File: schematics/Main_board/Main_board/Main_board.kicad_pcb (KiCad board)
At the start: 2 copper layers, 7 parts, among them J1 USB_B_Micro, J2 Conn_01x16_Female, U1 ESP32-S3-WROOM-1, U2 AP2112K-3.3, U3 AP9101CK6, U4 CH340G, U5 PCF8563T

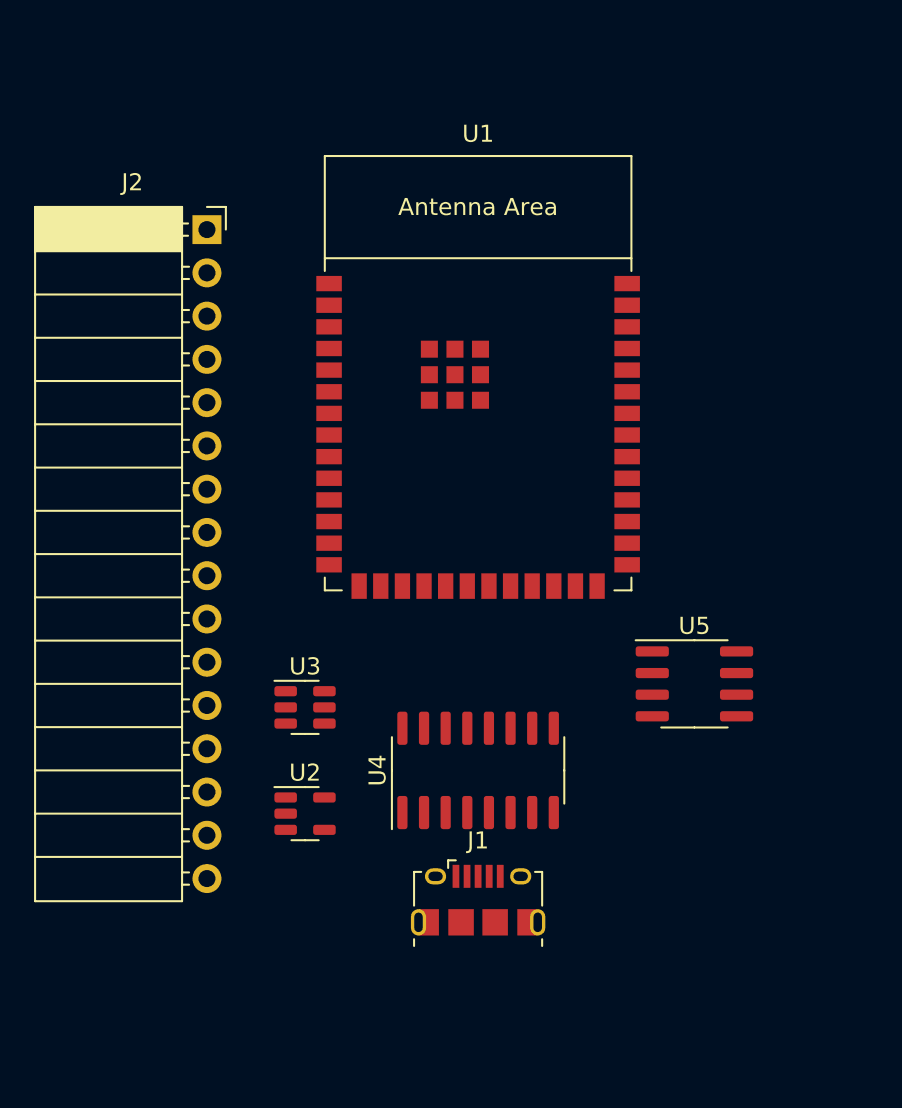
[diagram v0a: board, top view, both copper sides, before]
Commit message: Update: Added LCD symbol
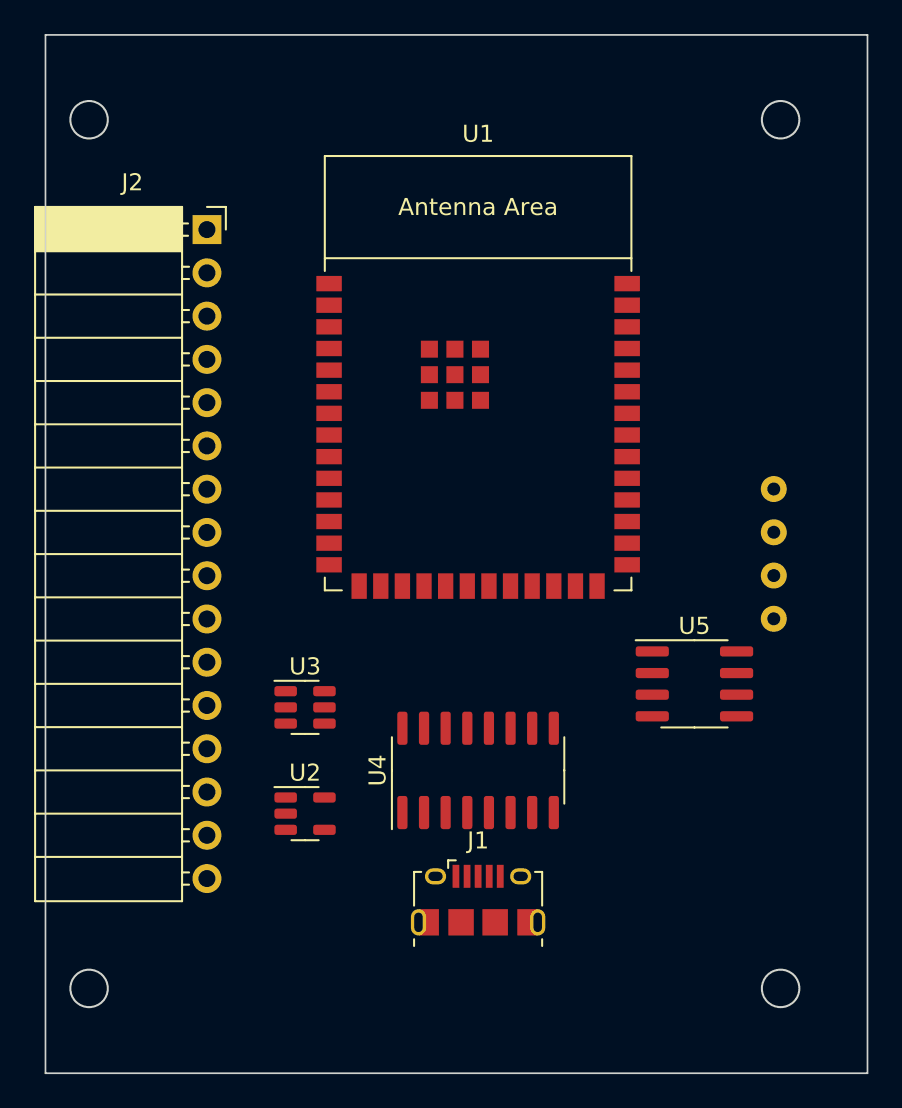
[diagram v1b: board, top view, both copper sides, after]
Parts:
- added U6: LCD, LCD:LCD_IIC_12864, B.Cu at (124.5, 73.7)
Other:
- board outline added: 48.3 x 61 mm
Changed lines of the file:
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@@
   (net 95 "unconnected-(U5-Pad7)")
   (net 96 "unconnected-(U5-Pad8)")
+  (net 97 "unconnected-(U6-Pad1)")
+  (net 98 "unconnected-(U6-Pad2)")
+  (net 99 "unconnected-(U6-Pad3)")
+  (net 100 "unconnected-(U6-Pad4)")
   (footprint "Connector_PinSocket_2.54mm:PinSocket_1x16_P2.54mm_Horizontal" (layer "F.Cu")
     (at 111.08 54.61)
@@
     (pad "6" thru_hole oval (at -2.5 -1.4) (size 1.25 0.95) (drill oval 0.85 0.55) (layers *.Cu *.Mask)
       (net 45 "unconnected-(J1-Pad6)") (pinfunction "Shield") (pintype "passive"))
-    (model "${KICAD6_3DMODEL_DIR}/Connector_USB.3dshapes/USB_Micro-B_Amphenol_10118194_Horizontal.wrl"
-      (offset (xyz 0 0 0))
-      (scale (xyz 1 1 1))
-      (rotate (xyz 0 0 0))
-    )
   )
   (footprint "Package_SO:SOIC-16_3.9x9.9mm_P1.27mm" (layer "F.Cu")
@@
     )
   )
+  (footprint "LCD:LCD_IIC_12864" (layer "B.Cu")
+    (at 124.46 73.66 90)
+    (property "Sheetfile" "Main_board.kicad_sch")
+    (property "Sheetname" "")
+    (attr through_hole)
+    (fp_text reference "U6" (at 0 0.5 270 unlocked) (layer "B.SilkS")
+      (effects (font (size 1 1) (thickness 0.15)) (justify mirror))
+    )
+    (fp_text value "LCD" (at 0 -1 270 unlocked) (layer "B.Fab")
+      (effects (font (size 1 1) (thickness 0.15)) (justify mirror))
+    )
+    (fp_text user "LCD SCREEN 128 64" (at 0 -5.08 270 unlocked) (layer "B.SilkS")
+      (effects (font (size 1 1) (thickness 0.15)) (justify mirror))
+    )
+    (fp_text user "${REFERENCE}" (at 0 -2.5 270 unlocked) (layer "B.Fab")
+      (effects (font (size 1 1) (thickness 0.15)) (justify mirror))
+    )
+    (fp_rect (start -26.8 17.78) (end 26.8 -17.78) (layer "B.SilkS") (width 0.12) (fill none))
+    (fp_rect (start -28.5 22.8) (end 28.5 -22.8) (layer "B.SilkS") (width 0.12) (fill none))
+    (fp_circle (center 25.5 20.3) (end 26.6 20.3) (layer "Edge.Cuts") (width 0.12) (fill solid))
+    (fp_circle (center -25.5 -20.3) (end -24.4 -20.3) (layer "Edge.Cuts") (width 0.12) (fill solid))
+    (fp_circle (center 25.5 -20.3) (end 26.6 -20.3) (layer "Edge.Cuts") (width 0.12) (fill solid))
+    (fp_circle (center -25.5 20.3) (end -24.4 20.3) (layer "Edge.Cuts") (width 0.12) (fill solid))
+    (pad "1" thru_hole circle (at -3.8 19.9 90) (size 1.524 1.524) (drill 0.762) (layers *.Cu *.Mask)
+      (net 97 "unconnected-(U6-Pad1)") (pinfunction "SDA") (pintype "input"))
+    (pad "2" thru_hole circle (at -1.26 19.9 90) (size 1.524 1.524) (drill 0.762) (layers *.Cu *.Mask)
+      (net 98 "unconnected-(U6-Pad2)") (pinfunction "SCL") (pintype "input"))
+    (pad "3" thru_hole circle (at 3.82 19.9 90) (size 1.524 1.524) (drill 0.762) (layers *.Cu *.Mask)
+      (net 99 "unconnected-(U6-Pad3)") (pinfunction "GND") (pintype "power_in"))
+    (pad "4" thru_hole circle (at 1.28 19.9 90) (size 1.524 1.524) (drill 0.762) (layers *.Cu *.Mask)
+      (net 100 "unconnected-(U6-Pad4)") (pinfunction "Vcc") (pintype "power_in"))
+    (model "/home/jose/Documentos/Projects/Watchdog/ESP32-watchdog/3dComponents/LCD screen-Part.step"
+      (offset (xyz 0 0 2.5))
+      (scale (xyz 1 1 1))
+      (rotate (xyz 0 0 0))
+    )
+  )
+  (gr_rect (start 101.6 43.18) (end 149.86 104.14) (layer "Edge.Cuts") (width 0.1) (fill none))
 )

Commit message: Update: added new schematics components
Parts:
- added BT1: 1v5 LR44, LCD:MY-LR44-02, B.Cu at (137.2, 111.3)
- added C1: 1uf, Capacitor_SMD:C_0201_0603Metric, F.Cu at (139.7, 62.7)
- added C2: 1uf, Capacitor_SMD:C_0201_0603Metric, F.Cu at (142.2, 59.2)
- added C3: 1uf, Capacitor_SMD:C_0201_0603Metric, F.Cu at (142.2, 61.0)
- added C4: 33p, Capacitor_SMD:C_0201_0603Metric, F.Cu at (139.7, 59.2)
- added C5: 33p, Capacitor_SMD:C_0201_0603Metric, F.Cu at (142.2, 62.7)
- added C6: 0.1u, Capacitor_SMD:C_0201_0603Metric, F.Cu at (139.7, 61.0)
- added C7: 0.1u, Capacitor_SMD:C_0201_0603Metric, F.Cu at (144.6, 59.2)
- added U7: LIS3DH, Package_LGA:LGA-16_3x3mm_P0.5mm_LayoutBorder3x5y, F.Cu at (144.8, 66.0)
- added Y1: 12Mhz, Crystal:Resonator_SMD_Murata_CSTxExxV-3Pin_3.0x1.1mm_HandSoldering, F.Cu at (140.7, 88.9)
- added Y2: 32.768kHz, Crystal:Crystal_C38-LF_D3.0mm_L8.0mm_Horizontal, F.Cu at (114.3, 40.6)
- U3: value AP9101CK6 -> BQ21040DBVR
- moved U1 12.7 mm to (127.0, 53.3)
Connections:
- J1 pad 1: unconnected-(J1-Pad1) -> +5V
- J1 pad 2: unconnected-(J1-Pad2) -> /D-
- J1 pad 3: unconnected-(J1-Pad3) -> /D+
- J1 pad 4: unconnected-(J1-Pad4) -> GNDREF
- J1 pad 5: unconnected-(J1-Pad5) -> GNDREF
- J1 pad 6: unconnected-(J1-Pad6) -> GNDREF
- J2 pad 1: unconnected-(J2-Pad1) -> +3V3
- J2 pad 10: unconnected-(J2-Pad10) -> /I/O_1
- J2 pad 11: unconnected-(J2-Pad11) -> /I/O_2
- J2 pad 12: unconnected-(J2-Pad12) -> /I/O_3
- J2 pad 13: unconnected-(J2-Pad13) -> /I/O_4
- J2 pad 14: unconnected-(J2-Pad14) -> /I/O_5
- J2 pad 15: unconnected-(J2-Pad15) -> GNDREF
- J2 pad 16: unconnected-(J2-Pad16) -> GNDREF
- J2 pad 2: unconnected-(J2-Pad2) -> +3V3
- J2 pad 3: unconnected-(J2-Pad3) -> /UART_TX
- J2 pad 4: unconnected-(J2-Pad4) -> /UART_RX
- J2 pad 5: unconnected-(J2-Pad5) -> /MOSI
- J2 pad 6: unconnected-(J2-Pad6) -> /MISO
- J2 pad 7: unconnected-(J2-Pad7) -> /CLK
- J2 pad 8: unconnected-(J2-Pad8) -> /SDA_2
- J2 pad 9: unconnected-(J2-Pad9) -> /SCL_2
- U1 pad 36: unconnected-(U1-Pad36) -> /UART_TX0_PGR
- U1 pad 37: unconnected-(U1-Pad37) -> /UART_RX0_PGR
- U2 pad 1: unconnected-(U2-Pad1) -> +BATT
- U2 pad 2: unconnected-(U2-Pad2) -> GNDREF
- U2 pad 3: unconnected-(U2-Pad3) -> +BATT
- U2 pad 5: unconnected-(U2-Pad5) -> +3V3
- U3 pad 5: unconnected-(U3-Pad5) -> Net-(C3-Pad1)
- U3 pad 6: unconnected-(U3-Pad6) -> GNDREF
- U4 pad 1: unconnected-(U4-Pad1) -> GNDREF
- U4 pad 16: unconnected-(U4-Pad16) -> +5V
- U4 pad 2: unconnected-(U4-Pad2) -> /UART_TX0_PGR
- U4 pad 3: unconnected-(U4-Pad3) -> /UART_RX0_PGR
- U4 pad 4: unconnected-(U4-Pad4) -> Net-(C6-Pad2)
- U4 pad 5: unconnected-(U4-Pad5) -> /D+
- U4 pad 6: unconnected-(U4-Pad6) -> /D-
- U4 pad 7: unconnected-(U4-Pad7) -> Net-(C5-Pad1)
- U4 pad 8: unconnected-(U4-Pad8) -> Net-(C4-Pad1)
- U6 pad 1: unconnected-(U6-Pad1) -> /SDA_1
- U6 pad 2: unconnected-(U6-Pad2) -> /SCL_1
- U6 pad 3: unconnected-(U6-Pad3) -> GNDREF
- U6 pad 4: unconnected-(U6-Pad4) -> +3V3
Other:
- board size 48.3 x 61 mm -> 48.3 x 78.7 mm
- copper layers 2 -> 4

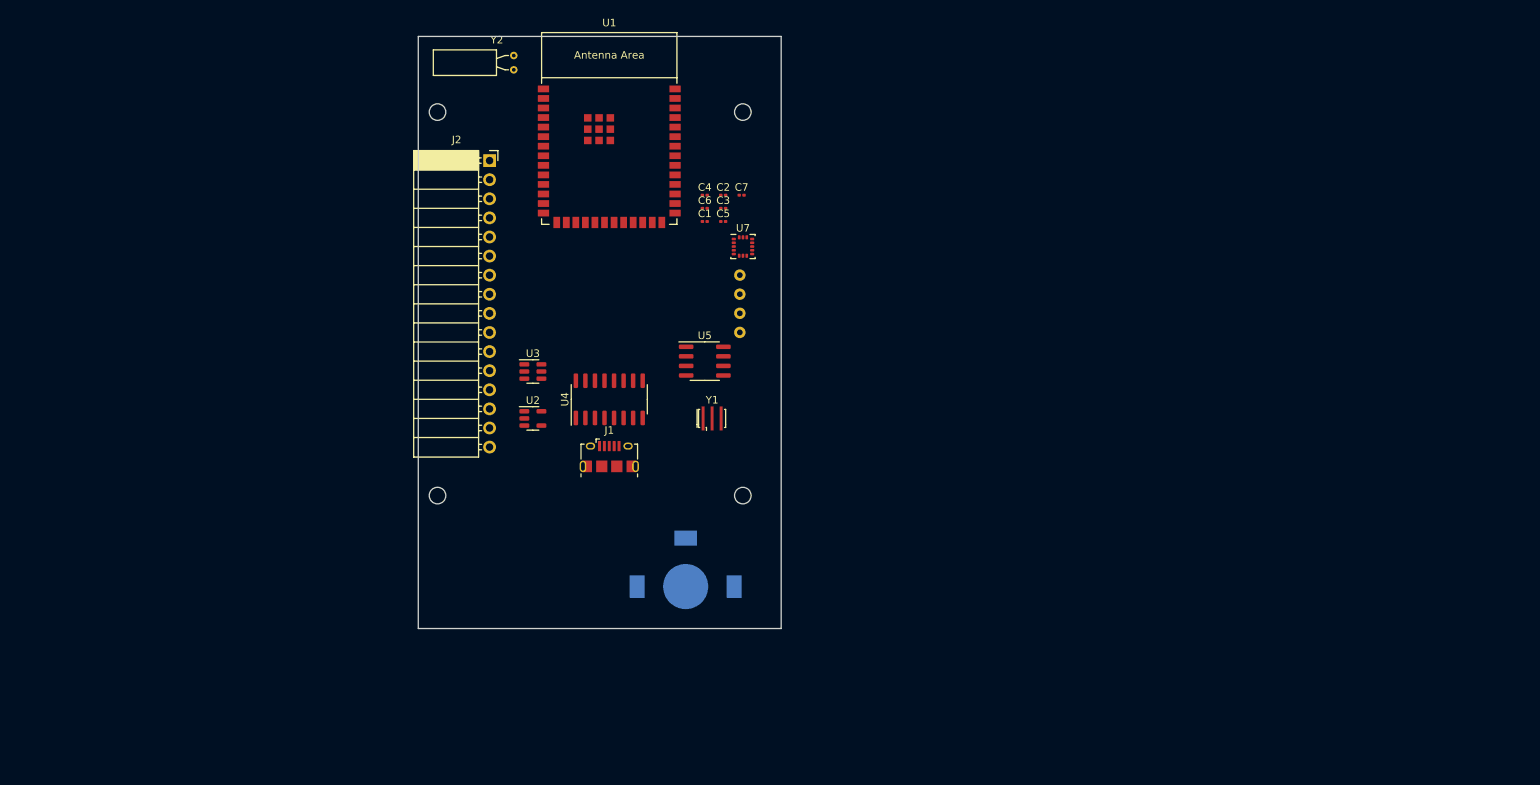
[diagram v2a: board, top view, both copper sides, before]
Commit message: Update: add components to schematics
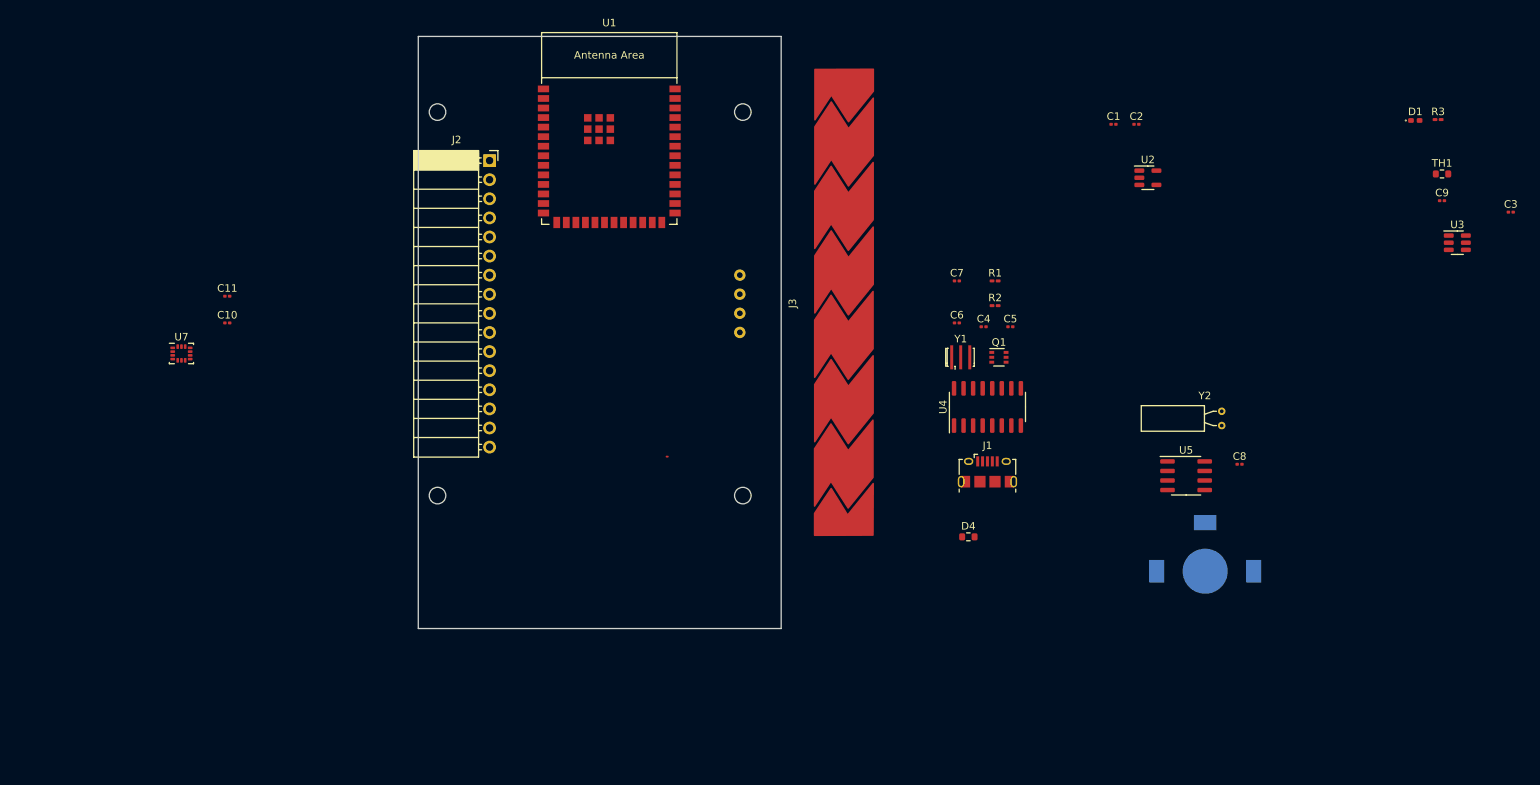
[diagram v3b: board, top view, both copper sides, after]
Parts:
- added C10: 100nf, Capacitor_SMD:C_0201_0603Metric, F.Cu at (76.2, 76.2)
- added C11: 100nf, Capacitor_SMD:C_0201_0603Metric, F.Cu at (76.2, 72.6)
- added C8: 8p, Capacitor_SMD:C_0201_0603Metric, F.Cu at (210.8, 95.0)
- added C9: 1uf, Capacitor_SMD:C_0201_0603Metric, F.Cu at (237.7, 59.9)
- added D1: LED, LED_SMD:LED_0402_1005Metric_Pad0.77x0.64mm_HandSolder, F.Cu at (234.2, 49.3)
- added D4: TPD1E10B06DPYR, Resistor_SMD:R_0603_1608Metric, F.Cu at (174.8, 104.6)
- added J3: TOUCH, LCD:slide_sensor_8p, F.Cu at (159.5, 73.7)
- added Q1: UMH3N, Package_TO_SOT_SMD:SOT-363_SC-70-6, F.Cu at (178.8, 80.8)
- added R1: 1K, Resistor_SMD:R_0201_0603Metric_Pad0.64x0.40mm_HandSolder, F.Cu at (178.3, 70.6)
- added R2: 10k, Resistor_SMD:R_0201_0603Metric_Pad0.64x0.40mm_HandSolder, F.Cu at (178.3, 73.9)
- added R3: 120, Resistor_SMD:R_0201_0603Metric_Pad0.64x0.40mm_HandSolder, F.Cu at (237.2, 49.2)
- added TH1: NCP18XH103F03RB, Resistor_SMD:R_0603_1608Metric, F.Cu at (237.7, 56.4)
- U7: value LIS3DH -> LSM6DS3; footprint Package_LGA:LGA-16_3x3mm_P0.5mm_LayoutBorder3x5y -> Package_LGA:LGA-14_3x2.5mm_P0.5mm_LayoutBorder3x4y
- moved U3 124.1 mm to (239.8, 65.5)
- moved Y2 105.4 mm to (208.4, 88.0)
- moved C3 104.7 mm to (246.9, 61.5)
- moved U2 87.8 mm to (198.6, 56.9)
- moved U7 76.0 mm to (70.1, 80.3)
- moved BT1 69.1 mm to (206.2, 109.2)
- moved U5 65.8 mm to (203.7, 96.5)
- moved C1 55.9 mm to (194.1, 49.8)
- moved C2 55.8 mm to (197.1, 49.8)
- moved J1 50.3 mm to (177.3, 96.0)
- moved U4 50.3 mm to (177.3, 87.4)
- moved C4 41.0 mm to (176.8, 76.7)
- moved C5 40.7 mm to (180.3, 76.7)
- moved C6 36.8 mm to (173.2, 76.2)
- moved Y1 34.0 mm to (173.7, 80.8)
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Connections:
- net /CLK renamed /SPI_CLK
- BT1 pad 1: unconnected-(BT1-Pad1) -> Net-(BT1-Pad1)
- BT1 pad 2: unconnected-(BT1-Pad2) -> GNDREF
- J2 pad 8: /SDA_2 -> /SDA_1
- J2 pad 9: /SCL_2 -> /SCL_1
- U1 pad 10: unconnected-(U1-Pad10) -> /UART_TX
- U1 pad 11: unconnected-(U1-Pad11) -> /UART_RX
- U1 pad 15: unconnected-(U1-Pad15) -> /I/O_3
- U1 pad 23: unconnected-(U1-Pad23) -> /SCL_1
- U1 pad 26: unconnected-(U1-Pad26) -> /SDA_1
- U1 pad 27: unconnected-(U1-Pad27) -> /BOOT0
- U1 pad 3: unconnected-(U1-Pad3) -> /EN
- U1 pad 38: unconnected-(U1-Pad38) -> /I/O_2
- U1 pad 39: unconnected-(U1-Pad39) -> /I/O_1
- U1 pad 4: unconnected-(U1-Pad4) -> /I/O_4
- U1 pad 5: unconnected-(U1-Pad5) -> /I/O_5
- U3 pad 1: unconnected-(U3-Pad1) -> Net-(TH1-Pad1)
- U3 pad 2: unconnected-(U3-Pad2) -> Net-(C9-Pad2)
- U3 pad 3: unconnected-(U3-Pad3) -> /NCH_CH_PIN
- U4 pad 13: unconnected-(U4-Pad13) -> /DTR
- U4 pad 14: unconnected-(U4-Pad14) -> /RTS
- U5 pad 1: unconnected-(U5-Pad1) -> Net-(C8-Pad1)
- U5 pad 2: unconnected-(U5-Pad2) -> Net-(U5-Pad2)
- U5 pad 3: unconnected-(U5-Pad3) -> /INT_ALARM
- U5 pad 4: unconnected-(U5-Pad4) -> GNDREF
- U5 pad 5: unconnected-(U5-Pad5) -> /SDA_1
- U5 pad 6: unconnected-(U5-Pad6) -> /SCL_1
- U5 pad 7: unconnected-(U5-Pad7) -> /1hz_CLKOUT
- U5 pad 8: unconnected-(U5-Pad8) -> Net-(BT1-Pad1)
- U7 pad 10: Net-(U7-Pad10) -> unconnected-(U7-Pad10)
- U7 pad 12: Net-(U7-Pad10) -> unconnected-(U7-Pad12)
- U7 pad 13: unconnected-(U7-Pad13) -> /SCL_1
- U7 pad 14: unconnected-(U7-Pad14) -> /SDA_1
- U7 pad 2: unconnected-(U7-Pad2) -> GNDREF
- U7 pad 3: unconnected-(U7-Pad3) -> GNDREF
- U7 pad 5: Net-(U7-Pad10) -> Net-(C10-Pad1)
- U7 pad 6: unconnected-(U7-Pad6) -> GNDREF
- U7 pad 7: unconnected-(U7-Pad7) -> GNDREF
- U7 pad 8: unconnected-(U7-Pad8) -> Net-(C11-Pad2)
- Y2 pad 1: unconnected-(Y2-Pad1) -> Net-(C8-Pad1)
- Y2 pad 2: unconnected-(Y2-Pad2) -> Net-(U5-Pad2)
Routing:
- net (no net): track 0.00 -> 0.51 mm
